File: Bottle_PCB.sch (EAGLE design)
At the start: 81 parts, among them J1 GROVE-4P-2.0-SMD, Q1 8.000 MHz, Q5 ZVN 3306 F, Q6 ZVN 3306 F, Q7 ZVN 3306 F, U1 USD-SOCKETNEW

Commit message: - employed several more libraries from Seed Studio and Arduino Project - replaced power supply with modern solution, charging circuitry etc.
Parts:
- removed C_U12V: 100µF/16V, _E:CPOL-EUSMCD
- removed C_U5V: 100µF/6,3V, _E:CPOL-EUSMCD
- removed D_U5V: MBRS120, _D:D_SMB
- removed LM2594_3.3: LM2594, _Voltage_Regulators:LM2594
- removed L_U5V: 100µH, _Trafo_Spule:L_PISM
- removed R_U12V: 10k, quantum-sensor:R-R0805
- removed SV2, SV3: (no value), con-ml:ML10L
- removed T_U12V: (no value), _transistor:MOS_P_SOT23_GDS
- removed VIN: AK350/2, con-ptr500:AK350/2
- added C13: 1µF, rcl:C-EUC0805
- added C14, C15: 100nF, resistor:C-EUC0603
- added C_3V3, C_VIN, C_V_LIPO_USB: 10µ/10V, _E:CPOL-EUSMCD
- added D2, D3, D4: MSS1P2U, Seed-Discrete:D1005
- added IC1: LP2985-33DBV, Arduino-SmartPrj:LP2985-XXDBVR33
- added LED1: CHRG_Red, led:LEDCHIPLED_0603
- added LED2: DONE_Green, led:LEDCHIPLED_0603
- added LIPO-BAT, SOLAR: (no value), Seed-Battery-Connector:JACK-JST-2P-PW2.0
- added R1, R16: 10k, rcl:R-EU_R0603
- added R17: 330 (20mA) or 2k, rcl:R-EU_R0603
- added R18, R19: 2M_1%, rcl:R-EU_R0603
- added R20, R21: 10M_1%, rcl:R-EU_R0603
- added SW_CHARGE_INDICATORS: (no value), switch-omron:10-XX
- added T_LIPO_USB: (no value), _transistor:MOS_P_SOT23_GDS
- added U3: CN3065-1320040P1, OPL:CN3065-1320040P1
- added UART1_C1: 10n, Arduino-SmartPrj:C-EUC0603
- R10: value 40k -> 10k; device rcl:R-EU_M1206 -> rcl:R-EU_R0603
- R11: device rcl:R-EU_M1206 -> rcl:R-EU_R0603
- SJ2, SJ4: device jumper:SJ -> jumper:SJ2W
- UART1_C10, UART1_C11, UART1_C2: device _C:C-EUC0805 -> Arduino-SmartPrj:C-EUC0603
- UART1_RX_LED, UART1_TX_LED: device led:LEDCHIPLED_0805 -> led:LEDCHIPLED_0603
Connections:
- net PB2_VBATT_AIN0 renamed PB2_AIN0
- net PB3_VBATT_AIN1 renamed PB3_AIN1
- removed net N$16: SJ1.2, U2.UART_RTS
- removed net N$17: SJ2.2, U2.UART_TX
- removed net N$19: SJ3.2, U2.UART_CTS
- removed net N$21: SJ5.2, U2.VCC
- removed net N$24: SJ8.2, U2.RESETB
- removed net N$25: SJ6.2, U2.PIO1
- removed net N$26: SJ7.2, U2.PIO0
- removed net PA4: AD.5, ATMEGA1284.(PCINT4/ADC4)PA4
- removed net PA5: AD.6, ATMEGA1284.(PCINT5/ADC5)PA5
- removed net SWITCH_OUT: D_U5V.C, LM2594_3.3.SW, L_U5V.1
- removed net VBATT: R10.2, R11.1
- new net N$22: R1.2, U3.ISET
- new net N$27: U3.H
- new net PA4_V_SOLAR: AD.5, ATMEGA1284.(PCINT4/ADC4)PA4, R19.1, R21.2
- new net PA5_V_LIPO: AD.6, ATMEGA1284.(PCINT5/ADC5)PA5, C14.2, C15.1, R18.1, R20.2
- new net PC4_!DONE: ATMEGA1284.(PCINT20/TDO)PC4, LED2.C, R11.1, U3.DONE
- new net PC5_!CHRG: ATMEGA1284.(PCINT21/TDI)PC5, LED1.C, R10.1, U3.CHRG
- new net V_LIPO: C13.2, LIPO-BAT.P$1, R20.1, T_LIPO_USB.D, U3.BAT, U3.FB
- new net V_LIPO_USB: C_V_LIPO_USB.+, D4.-, IC1.IN, IC1.ON/!OFF, SW_CHARGE_INDICATORS.P, SW_CHARGE_INDICATORS.P1, T_LIPO_USB.S
- new net V_SOLAR: D2.+, SOLAR.P$1
- net +3V3: now also C_3V3.+, IC1.OUT, R10.2, R11.2; no longer C_U5V.+, LM2594_3.3.FB, L_U5V.2, R2.1, SV2.1, SV2.3, SV3.1, SV3.3
- net +5V: now also D3.+, D4.+, R16.2, T_LIPO_USB.G
- net BEE_RESET: now also SJ8.2, U2.RESETB
- net BEE_STATUS: now also SJ6.2, U2.PIO1
- net BEE_VCC: now also SJ5.2, U2.VCC
- net FTDI_CTS: now also SJ3.2, U2.UART_CTS
- net FTDI_DTR: now also SJ7.2, U2.PIO0
- net FTDI_RTS: now also SJ1.2, U2.UART_RTS
- net GND: now also C13.1, C14.1, C15.2, C_3V3.-, C_VIN.-, C_V_LIPO_USB.-, IC1.GND, LIPO-BAT.P$2, R1.1, R16.1, R18.2, R19.2, SOLAR.P$2, U3.GND, U3.TEMP, UART1_C1.2; no longer C_U12V.-, C_U5V.-, D_U5V.A, LM2594_3.3.GND, LM2594_3.3.ON/OFF, R11.2, R_U12V.2, SV2.2, SV2.4, SV2.6, SV3.2, SV3.4, SV3.6, VIN1.KL
- net N$18: now also LED1.A, LED2.A, R17.1; no longer R_U12V.1, T_U12V.G
- net N$20: now also R17.2, SW_CHARGE_INDICATORS.S, SW_CHARGE_INDICATORS.S1; no longer SJ4.2, U2.UART_RX
- net N$3: now also IC1.NC/FB, UART1_C1.1; no longer T_U12V.D, VIN2.KL
- net N$31: now also R2.1
- net PD0_RXD0_USB: now also SJ2.2, SJ4.3, U2.UART_TX
- net PD1_TXD0_USB: now also SJ2.3, SJ4.2, U2.UART_RX
- net VIN: now also C_VIN.+, D2.-, D3.-, R21.1, U3.VIN; no longer C_U12V.+, LM2594_3.3.IN, R10.1, SV2.9, SV3.9, T_U12V.S
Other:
- note added: "(2mA) dep. on LEDs"
- note added: "3V3 Generation"
- note added: "LiPo Charging and Power Source Select"
- note added: "This Pins go to Main MCU"
- note removed: "Spannungsversorgung"
- moved on the sheet: R10, R11, R2

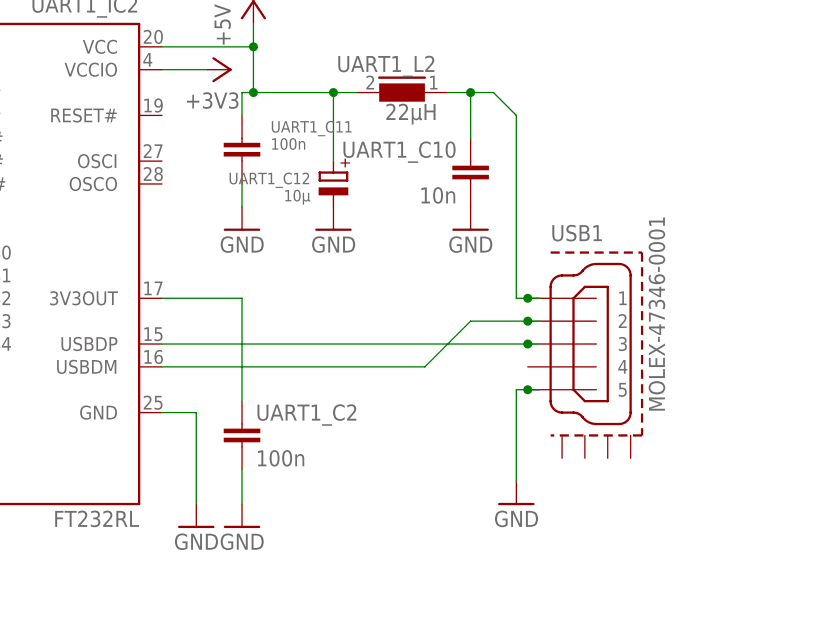
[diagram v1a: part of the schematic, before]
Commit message: - replaces mini USB B connector with SparkFun version
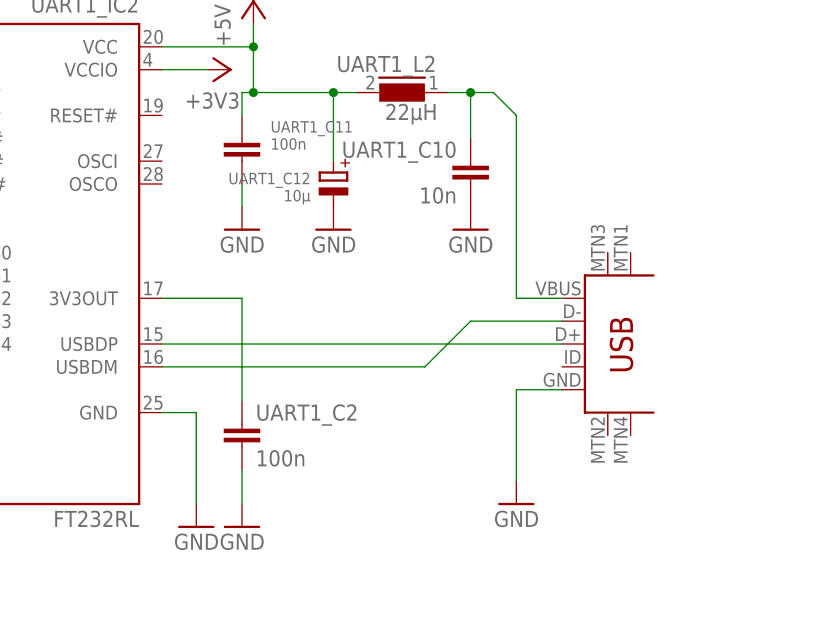
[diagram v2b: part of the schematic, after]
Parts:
- removed USB1: MOLEX-47346-0001, usb_con-update:MOLEX-47346-0001
- added U$1: USB-MINIB-5PIN, SparkFun-Connectors:USB-MINIB-5PIN
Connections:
- net GND: now also U$1.GND; no longer USB1.5
- net N$10: now also U$1.D+; no longer USB1.3
- net N$12: now also U$1.VBUS; no longer USB1.1
- net N$4: now also U$1.D-; no longer USB1.2
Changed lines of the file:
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@@
 <part name="UART1_L2" library="_Trafo_Spule" deviceset="L" device="_PIS2408" value="22µH"/>
 <part name="RESET_SW" library="switch-omron" deviceset="10-XX" device=""/>
-<part name="USB1" library="usb_con-update" deviceset="MOLEX-47346-0001" device=""/>
 <part name="D1" library="diode" deviceset="CGRM400*-G" device="" technology="1"/>
 <part name="C2" library="quantum-sensor" deviceset="C" device="-0805" value="100n"/>
@@
 <part name="C_V_LIPO_USB" library="_E" deviceset="CPOL-EU" device="SMCD" value="10µ/10V"/>
 <part name="UART1_C1" library="Arduino-SmartPrj" deviceset="C-EU" device="C0603" value="10n"/>
+<part name="U$1" library="SparkFun-Connectors" deviceset="USB-MINIB" device="-5PIN"/>
 </parts>
 <sheets>
@@
 <instance part="UART1_L2" gate="1" x="113.03" y="124.46" rot="MR0"/>
 <instance part="RESET_SW" gate="1" x="48.26" y="307.34" rot="R180"/>
-<instance part="USB1" gate="G$1" x="132.08" y="96.52"/>
 <instance part="D1" gate="G$1" x="30.48" y="322.58" rot="R90"/>
 <instance part="C2" gate="G$1" x="104.14" y="281.94" rot="R180"/>
@@
 <attribute name="VALUE" x="765.556" y="86.741" size="1.778" layer="96" rot="MR0"/>
 </instance>
+<instance part="U$1" gate="G$1" x="133.35" y="91.44"/>
 </instances>
 <busses>
@@
 <segment>
 <wire x1="125.73" y1="91.44" x2="125.73" y2="81.28" width="0.1524" layer="91"/>
-<wire x1="128.27" y1="91.44" x2="127" y2="91.44" width="0.1524" layer="91"/>
 <pinref part="GND3" gate="1" pin="GND"/>
-<pinref part="USB1" gate="G$1" pin="5"/>
-<wire x1="127" y1="91.44" x2="125.73" y2="91.44" width="0.1524" layer="91"/>
-<junction x="127" y="91.44"/>
+<wire x1="130.81" y1="91.44" x2="125.73" y2="91.44" width="0.1524" layer="91"/>
+<pinref part="U$1" gate="G$1" pin="GND"/>
 </segment>
 <segment>
@@
 <wire x1="86.36" y1="93.98" x2="115.57" y2="93.98" width="0.1524" layer="91"/>
 <wire x1="115.57" y1="93.98" x2="120.65" y2="99.06" width="0.1524" layer="91"/>
-<wire x1="120.65" y1="99.06" x2="127" y2="99.06" width="0.1524" layer="91"/>
+<wire x1="120.65" y1="99.06" x2="130.81" y2="99.06" width="0.1524" layer="91"/>
 <pinref part="UART1_IC2" gate="1" pin="USBDM"/>
-<pinref part="USB1" gate="G$1" pin="2"/>
-<wire x1="127" y1="99.06" x2="128.27" y2="99.06" width="0.1524" layer="91"/>
-<junction x="127" y="99.06"/>
+<pinref part="U$1" gate="G$1" pin="D-"/>
 </segment>
 </net>
 <net name="N$10" class="0">
 <segment>
-<wire x1="128.27" y1="96.52" x2="127" y2="96.52" width="0.1524" layer="91"/>
 <pinref part="UART1_IC2" gate="1" pin="USBDP"/>
-<pinref part="USB1" gate="G$1" pin="3"/>
-<wire x1="127" y1="96.52" x2="86.36" y2="96.52" width="0.1524" layer="91"/>
-<junction x="127" y="96.52"/>
+<wire x1="130.81" y1="96.52" x2="86.36" y2="96.52" width="0.1524" layer="91"/>
+<pinref part="U$1" gate="G$1" pin="D+"/>
 </segment>
 </net>
@@
 <wire x1="125.73" y1="101.6" x2="125.73" y2="121.92" width="0.1524" layer="91"/>
 <wire x1="125.73" y1="121.92" x2="123.19" y2="124.46" width="0.1524" layer="91"/>
-<wire x1="128.27" y1="101.6" x2="127" y2="101.6" width="0.1524" layer="91"/>
 <junction x="120.65" y="124.46"/>
 <pinref part="UART1_C10" gate="G$1" pin="1"/>
 <pinref part="UART1_L2" gate="1" pin="1"/>
-<pinref part="USB1" gate="G$1" pin="1"/>
-<wire x1="127" y1="101.6" x2="125.73" y2="101.6" width="0.1524" layer="91"/>
-<junction x="127" y="101.6"/>
+<wire x1="130.81" y1="101.6" x2="125.73" y2="101.6" width="0.1524" layer="91"/>
+<pinref part="U$1" gate="G$1" pin="VBUS"/>
 </segment>
 </net>

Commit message: - cleaned up and unified many discrete components - set Reichelt Order Numbers for all capacitors
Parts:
- removed D1: CGRM4001-G, diode:CGRM4001-G
- removed UART1_D_RESET: 1N4848, _D:D_MINIMELF
- added D5, D6: MSS1P2U, Seed-Discrete:D1005
- added R_WAKEUP: 10k, Arduino-SmartPrj:R-EU_R0603
- C1, C11, C12, C16, C2, C3, C4, C6, C7, C8, C9: device quantum-sensor:C-0805 -> Arduino-SmartPrj:C-EUC0603
- C10, C5: device rcl:CPOL-EUSMCD -> Arduino-SmartPrj:C-EUC1210
- C13: device rcl:C-EUC0805 -> Arduino-SmartPrj:C-EUC1210
- C14, C15: device resistor:C-EUC0603 -> Arduino-SmartPrj:C-EUC0603
- R1, R10, R11, R16, R17, R18, R19, R20, R21: device rcl:R-EU_R0603 -> Arduino-SmartPrj:R-EU_R0603
- R12, R13: value 4k7 -> 10k; device resistor:R-EU_R0603 -> Arduino-SmartPrj:R-EU_R0603
- R14, R15, R8, R9: device resistor:R-EU_R0603 -> Arduino-SmartPrj:R-EU_R0603
- R2, R3, R4, R5, R6, R7: device rcl:R-EU_M1206 -> Arduino-SmartPrj:R-EU_R0603
- R_RESET, UART1_R10, UART1_R7: device quantum-sensor:R-R0805 -> Arduino-SmartPrj:R-EU_R0603
- UART1_R6: device _R:R-EU_R0805 -> Arduino-SmartPrj:R-EU_R0603
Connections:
- new net N$16: C12.2, R_WAKEUP.1, SW_WAKEUP.P, SW_WAKEUP.P1
- net +3V3: now also D6.-; no longer D1.C
- net BEE_VCC: now also C10.1; no longer C10.+
- net FTDI_DTR: now also D5.-; no longer UART1_D_RESET.C
- net GND: now also C10.2, C5.2; no longer C10.-, C5.-
- net MCU_RST: now also D5.+, D6.+; no longer D1.A, UART1_D_RESET.A
- net N$31: now also C5.1; no longer C5.+
- net PB1_INT_BUTTON: no longer C12.2, SW_WAKEUP.P, SW_WAKEUP.P1
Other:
- moved on the sheet: C12, SW_WAKEUP

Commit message: - unified, replaced and checked all components - added vendor IDs and order information to all components - generated BOMs
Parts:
- removed C_3V3, C_VIN, C_V_LIPO_USB: 10µ/10V, _E:CPOL-EUSMCD
- removed UART1_C12: 10µ, _E:CPOL-EUSMCD
- added C17, C18, C19, C20: 10µF / 16V, Arduino-SmartPrj:C-EUC0805
- ATMEGA1284P-AU: value ATMEGA644A -> Reichelt ATMEGA 1284P-AU
- GROOVE_A6_A7, GROOVE_D7_D8, GROOVE_I2C: value GROVE-4P-2.0-SMD -> GROVE-4P-2.0-SMD Seed ACC39145O
- IC1: value LP2985-33DBV -> LP2985-33DBV, Farnell 2395925
- ISP1: value AVRISP-6 -> Reichelt WSL 6G
- Q1: value 8.000 MHz -> 16.000 MHz; device crystal:CRYSTALHC18U-V -> crystal:CRYSTALHC49U-V
- Q5, Q6, Q7: value ZVN 3306 F -> Reichelt ZVN 3306 F
- R17: value 330 (20mA) or 2k -> 330 (20mA) or 2k2
- R5: value 20k -> 10k
- T_LIPO_USB: value (none) -> Reichelt IRLML 6402
- U1: value USD-SOCKETNEW -> Sparkfun PRT-00127
- U2: value (none) -> Seed BLE Bee - Based on HM-11 Module sowie Bluetooth V4.0 HM-11 BLE Module
- U3: value CN3065-1320040P1 -> CN3065-1320040P1, Aliexpress Such as rhyme new original CN3065 DFN8 lithium battery charge management / protection chip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
- UART1_IC2: value FT232RL -> Reichelt FT 232 RL
- UART1_L2: device _Trafo_Spule:L_PIS2408 -> rcl:L-EUL1812
- UART1_R10, UART1_R7: value 1k -> 2k2
- USB_CONNECTOR: value USB-MINIB-5PIN -> USB-MINIB-5PIN Sparkfun PRT-00587
- XBEE_SOCKET: value XBEE-1B3 -> 2x Reichelt BL 1X10G SMD2,00
- renumbered ATMEGA1284 to ATMEGA1284P-AU, J1 to GROOVE_A6_A7, U$1 to USB_CONNECTOR
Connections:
- net +3V3: now also C18.1; no longer C_3V3.+
- net +5V: now also C20.1; no longer UART1_C12.+
- net GND: now also C17.2, C18.2, C19.2, C20.2; no longer C_3V3.-, C_VIN.-, C_V_LIPO_USB.-, UART1_C12.-
- net VIN: now also C19.1; no longer C_VIN.+
- net V_LIPO_USB: now also C17.1; no longer C_V_LIPO_USB.+

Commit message: - merged BOMs - BOM_Merged.csv is checked for correctness and completeness - minor adjustments in Device Values for unification
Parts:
- C1: value 22p -> 22pF
- C10, C5: value 1µ -> 1µF
- C11, C12, C2, C3, C4, C6, C7, C8, UART1_C11, UART1_C2: value 100n -> 100nF
- C9: value 22p -> 22pf
- UART1_C10: value 10n -> 10nF
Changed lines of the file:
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@@
 <variant name="BOM_CHECKED" value="Reichelt SMD-0603 10K"/>
 </part>
-<part name="C9" library="Arduino-SmartPrj" deviceset="C-EU" device="C0603" value="22p">
+<part name="C9" library="Arduino-SmartPrj" deviceset="C-EU" device="C0603" value="22pf">
 <variant name="BOM_CHECKED" value="Reichelt NPO-G0603 22P"/>
 </part>
-<part name="C1" library="Arduino-SmartPrj" deviceset="C-EU" device="C0603" value="22p">
+<part name="C1" library="Arduino-SmartPrj" deviceset="C-EU" device="C0603" value="22pF">
 <variant name="BOM_CHECKED" value="Reichelt NPO-G0603 22P"/>
 </part>
-<part name="C7" library="Arduino-SmartPrj" deviceset="C-EU" device="C0603" value="100n">
+<part name="C7" library="Arduino-SmartPrj" deviceset="C-EU" device="C0603" value="100nF">
 <variant name="BOM_CHECKED" value="Reichelt X7R-G0603 100N"/>
 </part>
@@
 <part name="GND6" library="supply1" deviceset="GND" device=""/>
 <part name="GND9" library="supply1" deviceset="GND" device=""/>
-<part name="C6" library="Arduino-SmartPrj" deviceset="C-EU" device="C0603" value="100n">
+<part name="C6" library="Arduino-SmartPrj" deviceset="C-EU" device="C0603" value="100nF">
 <variant name="BOM_CHECKED" value="Reichelt X7R-G0603 100N"/>
 </part>
 <part name="UART1_IC2" library="FTDI" deviceset="FT232R" device="L" value="Reichelt FT 232 RL"/>
 <part name="GND3" library="supply1" deviceset="GND" device=""/>
-<part name="UART1_C2" library="Arduino-SmartPrj" deviceset="C-EU" device="C0603" value="100n">
+<part name="UART1_C2" library="Arduino-SmartPrj" deviceset="C-EU" device="C0603" value="100nF">
 <variant name="BOM_CHECKED" value="Reichelt X7R-G0603 100N"/>
 </part>
 <part name="GND5" library="supply1" deviceset="GND" device=""/>
 <part name="GND11" library="supply1" deviceset="GND" device=""/>
-<part name="UART1_C10" library="Arduino-SmartPrj" deviceset="C-EU" device="C0603" value="10n">
+<part name="UART1_C10" library="Arduino-SmartPrj" deviceset="C-EU" device="C0603" value="10nF">
 <variant name="BOM_CHECKED" value="Reichelt X7R-G0603 10N"/>
 </part>
 <part name="GND17" library="supply1" deviceset="GND" device=""/>
-<part name="UART1_C11" library="Arduino-SmartPrj" deviceset="C-EU" device="C0603" value="100n">
+<part name="UART1_C11" library="Arduino-SmartPrj" deviceset="C-EU" device="C0603" value="100nF">
 <variant name="BOM_CHECKED" value="Reichelt X7R-G0603 100N"/>
 </part>
@@
 <variant name="BOM_CHECKED" value="Reichelt TASTER 3301"/>
 </part>
-<part name="C2" library="Arduino-SmartPrj" deviceset="C-EU" device="C0603" value="100n">
+<part name="C2" library="Arduino-SmartPrj" deviceset="C-EU" device="C0603" value="100nF">
 <variant name="BOM_CHECKED" value="Reichelt X7R-G0603 100N"/>
 </part>
-<part name="C3" library="Arduino-SmartPrj" deviceset="C-EU" device="C0603" value="100n">
+<part name="C3" library="Arduino-SmartPrj" deviceset="C-EU" device="C0603" value="100nF">
 <variant name="BOM_CHECKED" value="Reichelt X7R-G0603 100N"/>
 </part>
@@
 <variant name="BOM_CHECKED" value="Reichelt SMD-0603 100K"/>
 </part>
-<part name="C4" library="Arduino-SmartPrj" deviceset="C-EU" device="C0603" value="100n">
+<part name="C4" library="Arduino-SmartPrj" deviceset="C-EU" device="C0603" value="100nF">
 <variant name="BOM_CHECKED" value="Reichelt X7R-G0603 100N"/>
 </part>
 <part name="GND8" library="supply1" deviceset="GND" device=""/>
-<part name="C5" library="Arduino-SmartPrj" deviceset="C-EU" device="C1210" value="1µ">
+<part name="C5" library="Arduino-SmartPrj" deviceset="C-EU" device="C1210" value="1µF">
 <variant name="BOM_CHECKED" value="Reichelt X7R-G1210 1,0"/>
 </part>
@@
 </part>
 <part name="+3V9" library="supply1" deviceset="+3V3" device=""/>
-<part name="C8" library="Arduino-SmartPrj" deviceset="C-EU" device="C0603" value="100n">
+<part name="C8" library="Arduino-SmartPrj" deviceset="C-EU" device="C0603" value="100nF">
 <variant name="BOM_CHECKED" value="Reichelt X7R-G0603 100N"/>
 </part>
 <part name="GND14" library="supply1" deviceset="GND" device=""/>
-<part name="C10" library="Arduino-SmartPrj" deviceset="C-EU" device="C1210" value="1µ">
+<part name="C10" library="Arduino-SmartPrj" deviceset="C-EU" device="C1210" value="1µF">
 <variant name="BOM_CHECKED" value="Reichelt X7R-G1210 1,0"/>
 </part>
@@
 <part name="+3V11" library="supply1" deviceset="+3V3" device=""/>
 <part name="+3V13" library="supply1" deviceset="+3V3" device=""/>
-<part name="C12" library="Arduino-SmartPrj" deviceset="C-EU" device="C0603" value="100n">
+<part name="C12" library="Arduino-SmartPrj" deviceset="C-EU" device="C0603" value="100nF">
 <variant name="BOM_CHECKED" value="Reichelt X7R-G0603 100N"/>
 </part>
@@
 <variant name="BOM_CHECKED" value="Reichelt TASTER 3301"/>
 </part>
-<part name="C11" library="Arduino-SmartPrj" deviceset="C-EU" device="C0603" value="100n">
+<part name="C11" library="Arduino-SmartPrj" deviceset="C-EU" device="C0603" value="100nF">
 <variant name="BOM_CHECKED" value="Reichelt X7R-G0603 100N"/>
 </part>

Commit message: - replaced Diodes with lower quality version, as they are easier to get - added important BOM information
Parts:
- D2, D3, D4, D5, D6: value MSS1P2U -> MSS1P2L
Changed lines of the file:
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@@
 <setting verticaltext="up"/>
 </settings>
-<grid distance="0.1" unitdist="inch" unit="inch" style="lines" multiple="1" display="no" altdistance="0.05" altunitdist="inch" altunit="inch"/>
+<grid distance="0.1" unitdist="inch" unit="inch" style="lines" multiple="1" display="no" altdistance="0.01" altunitdist="inch" altunit="inch"/>
 <layers>
 <layer number="1" name="Top" color="4" fill="1" visible="no" active="no"/>
@@
 <variant name="BOM_CHECKED" value="Reichelt X7R-G1210 1,0"/>
 </part>
-<part name="D2" library="Seed-Discrete" deviceset="D*" device="1005" value="MSS1P2U">
+<part name="D2" library="Seed-Discrete" deviceset="D*" device="1005" value="MSS1P2L">
 <variant name="BOM_CHECKED" value="DigiKey MSS1P2U"/>
 </part>
-<part name="D3" library="Seed-Discrete" deviceset="D*" device="1005" value="MSS1P2U">
+<part name="D3" library="Seed-Discrete" deviceset="D*" device="1005" value="MSS1P2L">
 <variant name="BOM_CHECKED" value="DigiKey MSS1P2U"/>
 </part>
-<part name="D4" library="Seed-Discrete" deviceset="D*" device="1005" value="MSS1P2U">
+<part name="D4" library="Seed-Discrete" deviceset="D*" device="1005" value="MSS1P2L">
 <variant name="BOM_CHECKED" value="DigiKey MSS1P2U"/>
 </part>
@@
 <variant name="BOM_CHECKED" value="Reichelt SMD-0603 10K"/>
 </part>
-<part name="D5" library="Seed-Discrete" deviceset="D*" device="1005" value="MSS1P2U">
+<part name="D5" library="Seed-Discrete" deviceset="D*" device="1005" value="MSS1P2L">
 <variant name="BOM_CHECKED" value="DigiKey MSS1P2U"/>
 </part>
-<part name="D6" library="Seed-Discrete" deviceset="D*" device="1005" value="MSS1P2U">
+<part name="D6" library="Seed-Discrete" deviceset="D*" device="1005" value="MSS1P2L">
 <variant name="BOM_CHECKED" value="DigiKey MSS1P2U"/>
 </part>
